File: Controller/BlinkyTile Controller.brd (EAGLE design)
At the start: 40 x 25 mm, 26 parts, among them CON1 USB_MICROSMT+THRUHULE, Q1 CRYSTAL_4PAD2520, U1 MK20D--VFM5, U2 W25Q80BV150, U3 74LVC1G17DCK, U4 74LVC1G17DCK, U5 74LVC1G17DCK

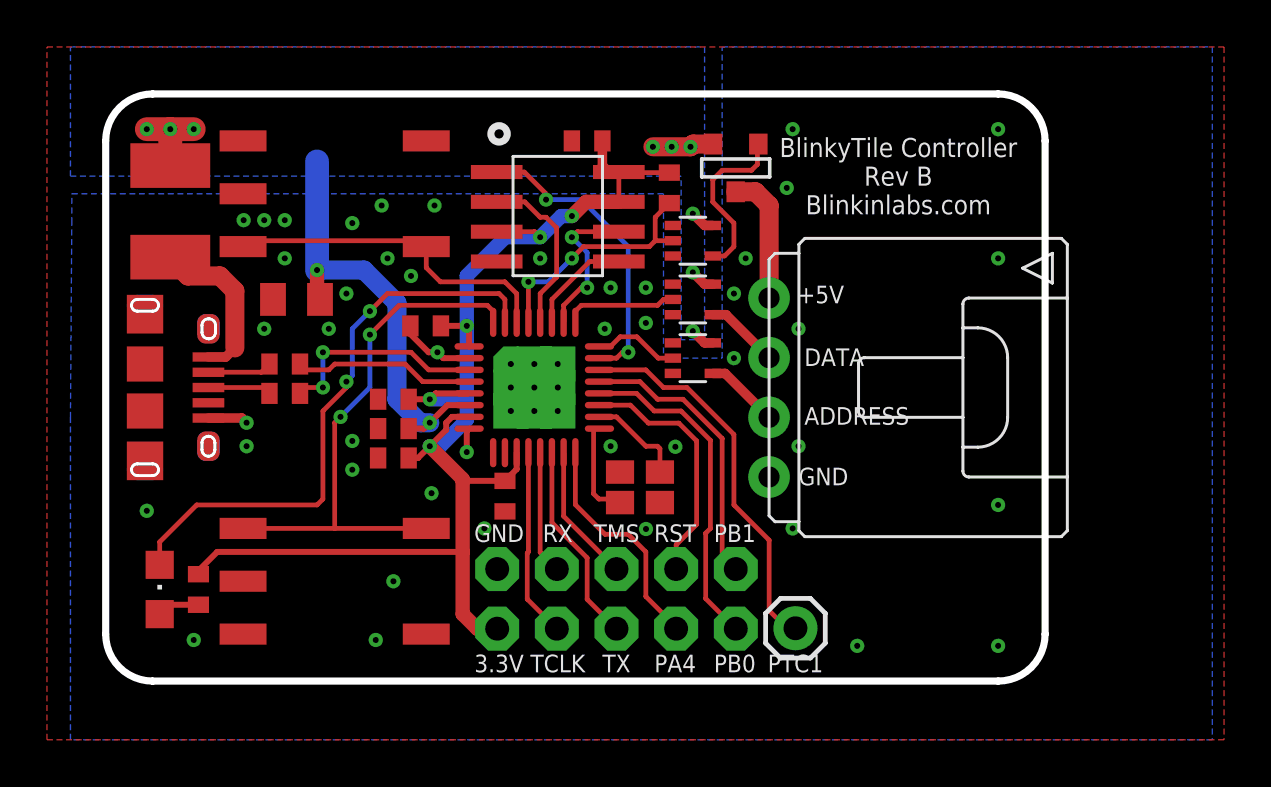
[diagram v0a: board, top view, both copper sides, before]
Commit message: Add ferrite beads, move the fuse to the ouput.
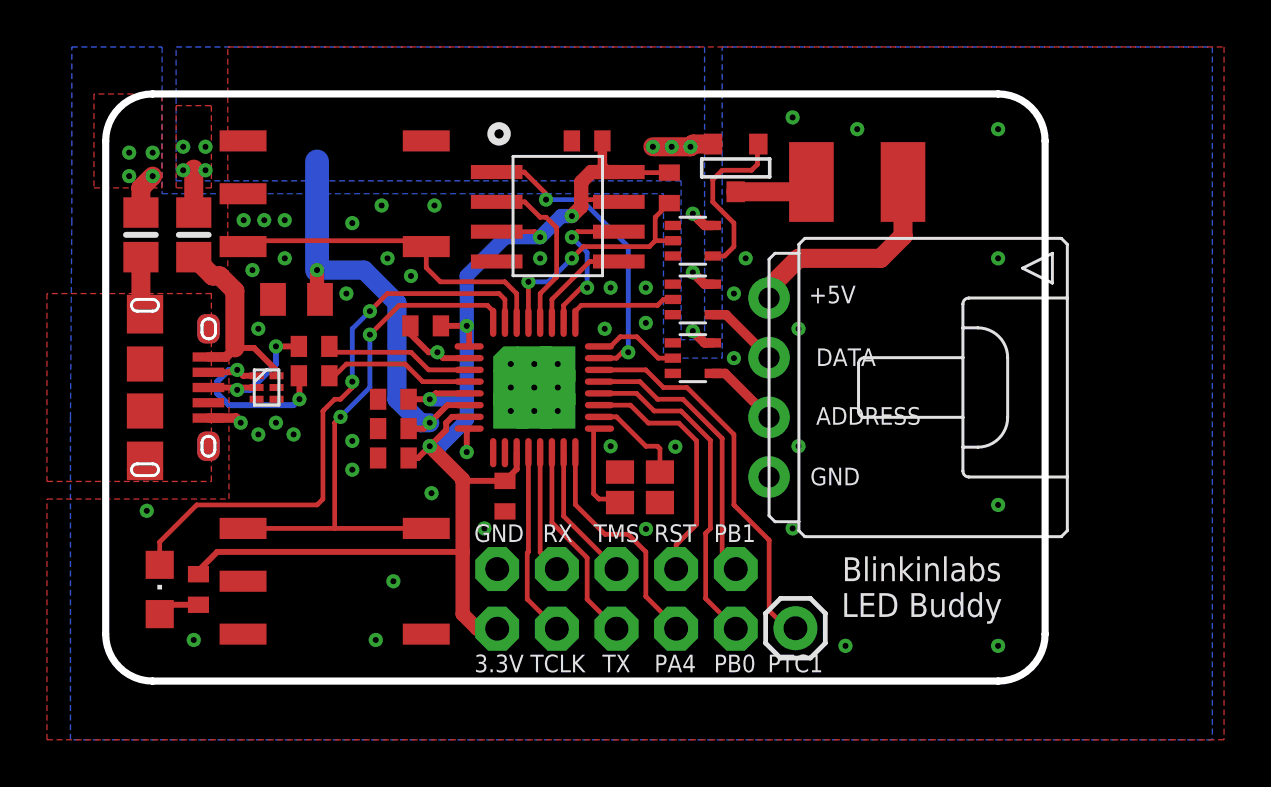
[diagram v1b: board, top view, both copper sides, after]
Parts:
- added L2, L3: FB0805/NO-OUTLINE, blinkinlabs:0805
- added U6: TPD4S012, blinkinlabs:R-PUSON-N6
- U2: value W25Q80BV150 -> W25Q--DVSN(150)
- moved L1 29.3 mm to (32.0, 8.75), turned to 0 degrees
- moved R2 2.36 mm to (8.88, 1.75)
- moved R1 1.35 mm to (8.88, 0.50)
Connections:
- removed net N$9: CON1.PIN$2, R1.1
- new net N$7: CON1.PIN$2, R1.1, U6.P$1
- new net N$8: L1.2, SV1.P$1
- new net SHIELD: CON1.PAD$1, CON1.PAD$10, CON1.PAD$2, CON1.PAD$3, CON1.PAD$4, CON1.PAD$5, CON1.PAD$6, CON1.PAD$7, CON1.PAD$8, CON1.PAD$9, L2.1
- net +5V: now also L3.1; no longer L1.2
- net GND: now also L2.2, U6.P$4
- net N$10: now also U6.P$2
- net N$3: now also L3.2, U6.P$6; no longer L1.1
- net N$5: now also L1.1; no longer SV1.P$1
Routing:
- net N$8: track 0.00 -> 9.35 mm
- net N$7: track 0.00 -> 8.57 mm, vias 0 -> 2
- net N$10: track 2.70 -> 5.96 mm, vias 0 -> 2
- net N$12: track 9.11 -> 6.36 mm, vias 2 -> 0
- net N$9: track 2.74 -> 0.00 mm
- net N$5: track 5.61 -> 3.40 mm
- net SHIELD: track 0.00 -> 2.12 mm
- net +5V: track 28.1 -> 26.4 mm, vias 11 -> 12
- net +3V3: track 57.3 -> 58.9 mm
- net GND: track 6.02 -> 7.53 mm, vias 45 -> 51
- net N$3: track 7.09 -> 8.46 mm
- net N$11: track 7.72 -> 6.47 mm
- added copper zone on layer 1, net +5V
- added copper zone on layer 1, net SHIELD
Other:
- board text added: "Blinkinlabs LED Buddy"
- board text added: "Blinkinlabs LED Buddy Rev C Blinkinlabs.com"
- board text removed: "BlinkyTile Controller Rev B Blinkinlabs.com"
- board text removed: "Thanks for using the BlinkyTile controller!"

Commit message: Tidy schematic and add values to ferrites, crystal
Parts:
- L2, L3: value FB0805/NO-OUTLINE -> 130ohm @100MHz
- Q1: value CRYSTAL_4PAD2520 -> 16MHz
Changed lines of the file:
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@@
 <attribute name="VALUE" x="4.84" y="-9.87" size="1.27" layer="27" rot="R90"/>
 </element>
-<element name="Q1" library="blinkinlabs" package="CRSYTAL_2520" value="CRYSTAL_4PAD2520" x="22.75" y="-4.25" smashed="yes" rot="R180"/>
+<element name="Q1" library="blinkinlabs" package="CRSYTAL_2520" value="16MHz" x="22.75" y="-4.25" smashed="yes" rot="R180"/>
 <element name="R1" library="adafruit" package="R0402" value="33" x="8.875" y="0.5" smashed="yes"/>
 <element name="R2" library="adafruit" package="R0402" value="33" x="8.875" y="1.75" smashed="yes"/>
@@
 <attribute name="VALUE" x="4.405" y="1.905" size="1.27" layer="27" ratio="10" rot="R270"/>
 </element>
-<element name="L3" library="blinkinlabs" package="0805" value="FB0805/NO-OUTLINE" x="3.75" y="6.5" smashed="yes" rot="R270">
+<element name="L3" library="blinkinlabs" package="0805" value="130ohm @100MHz" x="3.75" y="6.5" smashed="yes" rot="R270">
 <attribute name="VALUE" x="2.988" y="4.468" size="0.4064" layer="27" ratio="10" rot="R270"/>
 </element>
-<element name="L2" library="blinkinlabs" package="0805" value="FB0805/NO-OUTLINE" x="1.5" y="6.5" smashed="yes" rot="R90">
+<element name="L2" library="blinkinlabs" package="0805" value="130ohm @100MHz" x="1.5" y="6.5" smashed="yes" rot="R90">
 <attribute name="VALUE" x="2.262" y="8.532" size="0.4064" layer="27" ratio="10" rot="R90"/>
 </element>

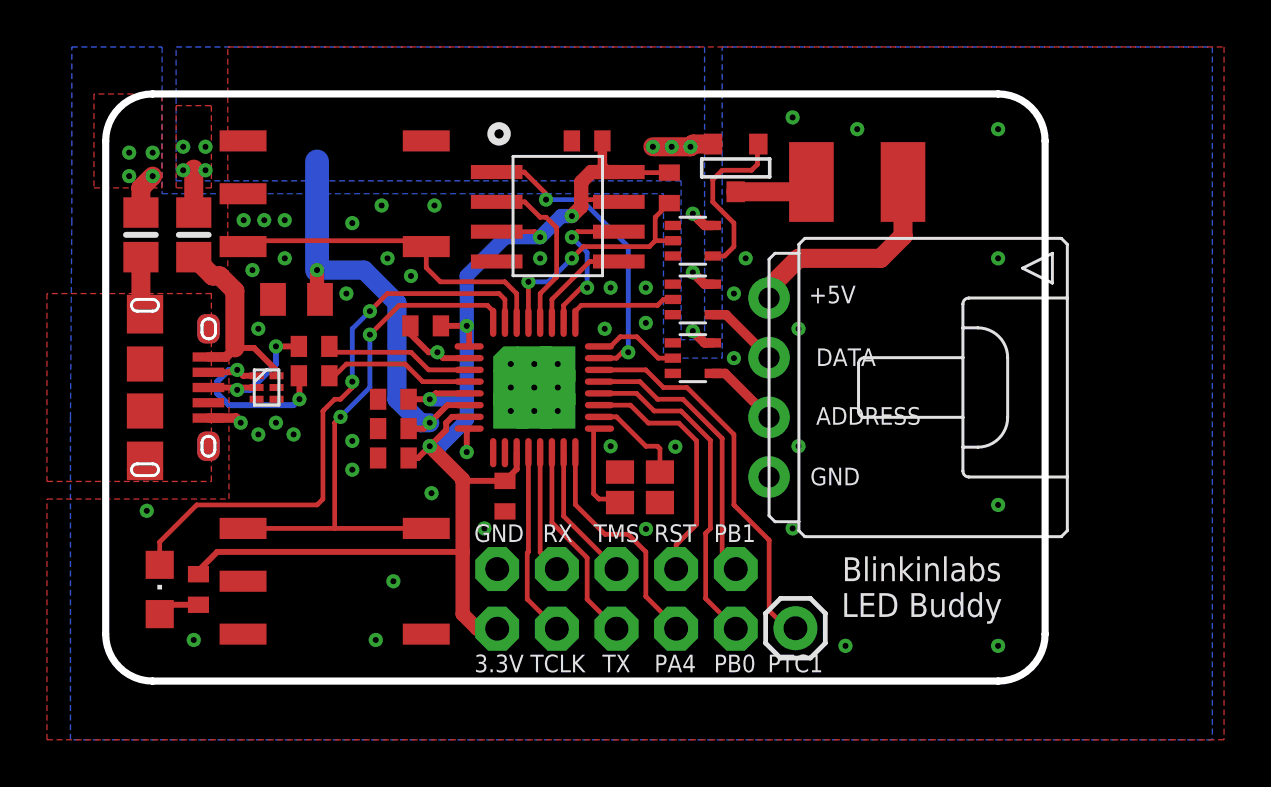
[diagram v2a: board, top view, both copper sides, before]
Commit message: Enlarge via sizes to .3mm
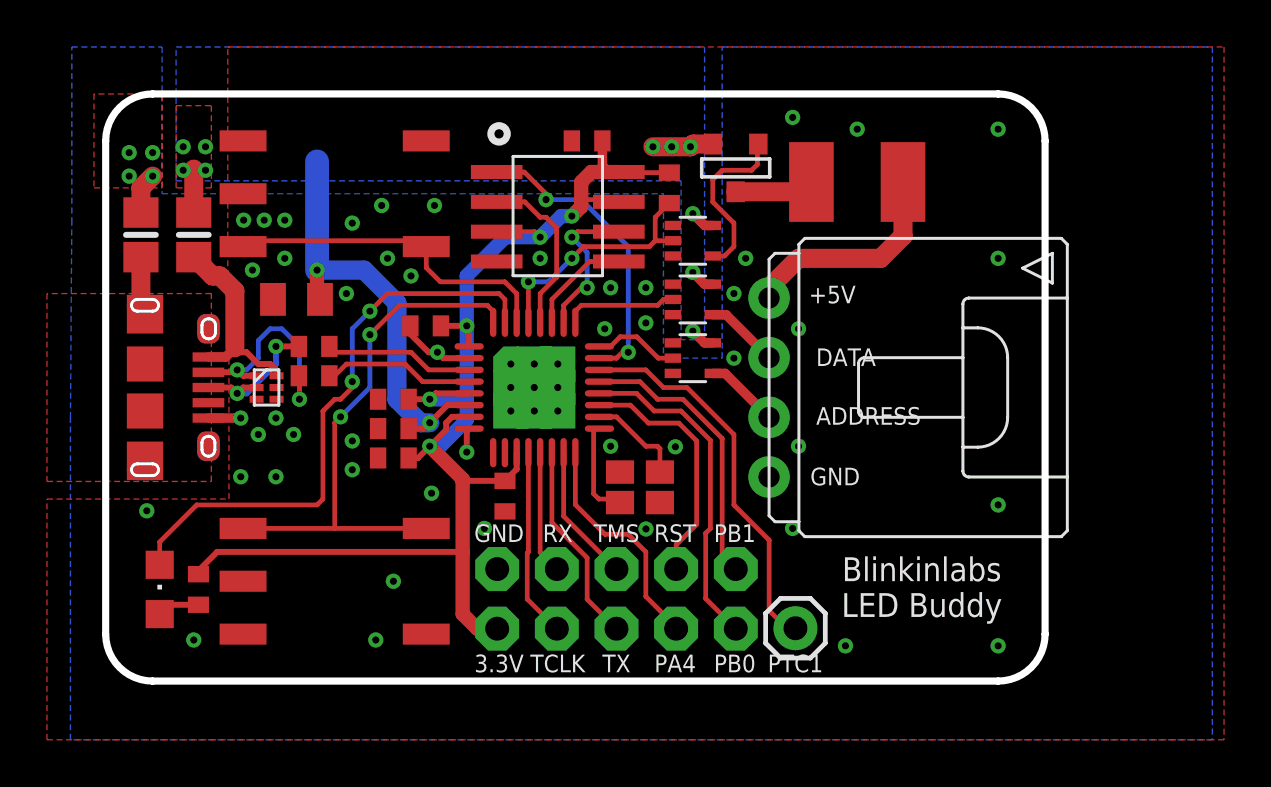
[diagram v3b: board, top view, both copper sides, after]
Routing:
- net N$7: track 8.57 -> 9.58 mm
- net GND: track 7.53 -> 7.45 mm, vias 51 -> 52

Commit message: Controller: Switch back to 208 package for flash chip
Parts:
- U2: value W25Q--DVSN(150) -> W25Q--DVSS(208); device blinkinlabs:SOIC8-150 -> blinkinlabs:SOIC8-208
- moved U2 0.15 mm to (19.1, 7.30)
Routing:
- net +3V3: track 58.9 -> 61.1 mm
- net FLASH_MISO: track 7.67 -> 9.55 mm
- net GND: track 7.45 -> 9.27 mm
- net FLASH_CS: track 12.9 -> 13.8 mm
- net FLASH_SCK: track 6.55 -> 7.19 mm
- net FLASH_MOSI: track 4.49 -> 5.13 mm
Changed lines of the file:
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@@
 <element name="R2" library="adafruit" package="R0402" value="33" x="8.875" y="1.75" smashed="yes"/>
 <element name="R4" library="adafruit" package="R0402" value="330" x="3.95" y="-8.6" smashed="yes" rot="R90"/>
-<element name="U2" library="blinkinlabs" package="SOIC8-150" value="W25Q--DVSN(150)" x="19.25" y="7.3" smashed="yes" rot="R270"/>
+<element name="U2" library="blinkinlabs" package="SOIC8-208" value="W25Q--DVSS(208)" x="19.1" y="7.3" smashed="yes" rot="R270"/>
 <element name="CON1" library="blinkinlabs" package="USB_MICRO_THRUHOLE" value="USB_MICROSMT+THRUHULE" x="1.675" y="0" smashed="yes" rot="R270"/>
 <element name="U4" library="74xx-little-us" package="SC70-5" value="74LVC1G17DCK" x="25" y="3.75" smashed="yes" rot="R270"/>
@@
 <via x="7.25" y="-3.8" extent="1-16" drill="0.3"/>
 <via x="5.75" y="-3.8" extent="1-16" drill="0.3"/>
+<wire x1="24.15" y1="5.6" x2="24.15" y2="5.4" width="0.2032" layer="1"/>
+<wire x1="24.15" y1="5.4" x2="23" y2="4.25" width="0.2032" layer="1"/>
 </signal>
 <signal name="N$2">
@@
 <wire x1="14.5" y1="-1.5" x2="14.5" y2="-1.8" width="0.254" layer="1"/>
 <wire x1="14.5" y1="-1.8" x2="13.8" y2="-2.5" width="0.254" layer="1"/>
-<wire x1="21.85" y1="9.175" x2="21.425" y2="9.175" width="0.4064" layer="1"/>
+<wire x1="22.49" y1="9.175" x2="21.425" y2="9.175" width="0.4064" layer="1"/>
 <wire x1="17.5" y1="-2.775" x2="17.5" y2="-3.475" width="0.254" layer="1"/>
 <wire x1="17.5" y1="-3.475" x2="17" y2="-3.975" width="0.254" layer="1"/>
@@
 <wire x1="15.81975" y1="-10.27" x2="15.2" y2="-9.65025" width="0.6096" layer="1"/>
 <via x="19.85" y="7.3" extent="1-16" drill="0.3"/>
-<wire x1="16.65" y1="6.635" x2="18.265" y2="6.635" width="0.2032" layer="1"/>
+<wire x1="15.71" y1="6.635" x2="18.265" y2="6.635" width="0.2032" layer="1"/>
 <wire x1="18.265" y1="6.635" x2="18.5" y2="6.4" width="0.2032" layer="1"/>
 <wire x1="19.85" y1="7.3" x2="19.4" y2="7.3" width="0.6096" layer="16"/>
@@
 <wire x1="15.375" y1="4.76" x2="17.015" y2="6.4" width="0.6096" layer="16"/>
 <wire x1="17.015" y1="6.4" x2="18.5" y2="6.4" width="0.6096" layer="16"/>
-<wire x1="21.85" y1="9.175" x2="21.875" y2="9.15" width="0.2032" layer="1"/>
-<wire x1="21.875" y1="9.15" x2="24" y2="9.15" width="0.2032" layer="1"/>
 <wire x1="21.425" y1="9.175" x2="21.15" y2="9.45" width="0.4064" layer="1"/>
 <wire x1="21.15" y1="9.45" x2="21.15" y2="10.5" width="0.4064" layer="1"/>
@@
 <wire x1="20.25" y1="8" x2="20.25" y2="8.75" width="0.6096" layer="1"/>
 <wire x1="20.25" y1="8.75" x2="20.675" y2="9.175" width="0.6096" layer="1"/>
-<wire x1="20.675" y1="9.175" x2="21.85" y2="9.175" width="0.6096" layer="1"/>
-<wire x1="21.85" y1="7.905" x2="21.755" y2="8" width="0.2032" layer="1"/>
-<wire x1="21.755" y1="8" x2="20.25" y2="8" width="0.2032" layer="1"/>
+<wire x1="20.675" y1="9.175" x2="22.49" y2="9.175" width="0.6096" layer="1"/>
+<wire x1="22.49" y1="9.175" x2="23.975" y2="9.175" width="0.2032" layer="1"/>
+<wire x1="23.975" y1="9.175" x2="24" y2="9.15" width="0.2032" layer="1"/>
+<wire x1="22.49" y1="7.905" x2="20.345" y2="7.905" width="0.2032" layer="1"/>
+<wire x1="20.345" y1="7.905" x2="20.25" y2="8" width="0.2032" layer="1"/>
 </signal>
 <signal name="TCLK">
@@
 <wire x1="22.25" y1="6" x2="20.25" y2="8" width="0.2032" layer="16"/>
 <wire x1="20.25" y1="8" x2="18.75" y2="8" width="0.2032" layer="16"/>
-<wire x1="16.65" y1="9.175" x2="17.825" y2="9.175" width="0.2032" layer="1"/>
+<wire x1="15.71" y1="9.175" x2="17.825" y2="9.175" width="0.2032" layer="1"/>
 <wire x1="17.825" y1="9.175" x2="18.75" y2="8.25" width="0.2032" layer="1"/>
 <wire x1="18.75" y1="8.25" x2="18.75" y2="8" width="0.2032" layer="1"/>
@@
 <via x="20.5" y="4.25" extent="1-16" drill="0.3"/>
 <via x="19.85" y="6.4" extent="1-16" drill="0.3"/>
-<wire x1="21.85" y1="6.635" x2="20.085" y2="6.635" width="0.2032" layer="1"/>
+<wire x1="22.49" y1="6.635" x2="20.085" y2="6.635" width="0.2032" layer="1"/>
 <wire x1="20.085" y1="6.635" x2="19.85" y2="6.4" width="0.2032" layer="1"/>
 <wire x1="20.5" y1="4.25" x2="20.5" y2="5.75" width="0.2032" layer="16"/>
@@
 <wire x1="19" y1="2.775" x2="19" y2="3.75" width="0.2032" layer="1"/>
 <wire x1="19" y1="3.75" x2="20.615" y2="5.365" width="0.2032" layer="1"/>
-<wire x1="21.85" y1="5.365" x2="20.615" y2="5.365" width="0.2032" layer="1"/>
+<wire x1="22.49" y1="5.365" x2="20.615" y2="5.365" width="0.2032" layer="1"/>
 </signal>
 <signal name="FLASH_MISO">
 <contactref element="U2" pad="2"/>
 <contactref element="U1" pad="28"/>
-<wire x1="17" y1="7.905" x2="16.65" y2="7.905" width="0.2032" layer="1"/>
+<wire x1="17" y1="7.905" x2="15.71" y2="7.905" width="0.2032" layer="1"/>
 <wire x1="18.5" y1="2.775" x2="18.5" y2="4" width="0.2032" layer="1"/>
 <wire x1="19.2" y1="4.7" x2="19.2" y2="6.8" width="0.2032" layer="1"/>
@@
 <wire x1="18.75" y1="7.25" x2="18.5" y2="7.25" width="0.2032" layer="1"/>
 <wire x1="18.5" y1="7.25" x2="17.845" y2="7.905" width="0.2032" layer="1"/>
-<wire x1="16.65" y1="7.905" x2="17.845" y2="7.905" width="0.2032" layer="1"/>
+<wire x1="15.71" y1="7.905" x2="17.845" y2="7.905" width="0.2032" layer="1"/>
 </signal>
 <signal name="STATUS">
@@
 <contactref element="R5" pad="1"/>
 <wire x1="18" y1="4.5" x2="18" y2="2.775" width="0.2032" layer="1"/>
-<wire x1="23.15" y1="6" x2="23.4" y2="6.25" width="0.2032" layer="1"/>
-<wire x1="23.4" y1="6.25" x2="24.15" y2="6.25" width="0.2032" layer="1"/>
-<wire x1="23.15" y1="6" x2="20.35" y2="6" width="0.2032" layer="1"/>
+<wire x1="23.45" y1="6.25" x2="24.15" y2="6.25" width="0.2032" layer="1"/>
 <wire x1="20.35" y1="6" x2="19.85" y2="5.5" width="0.2032" layer="1"/>
 <wire x1="18" y1="4.5" x2="18.85" y2="4.5" width="0.2032" layer="16"/>
 <wire x1="18.85" y1="4.5" x2="19.85" y2="5.5" width="0.2032" layer="16"/>
-<wire x1="24" y1="7.85" x2="23.4" y2="7.25" width="0.2032" layer="1"/>
-<wire x1="23.4" y1="7.25" x2="23.4" y2="6.25" width="0.2032" layer="1"/>
+<wire x1="23.45" y1="7.3" x2="23.45" y2="6.25" width="0.2032" layer="1"/>
+<wire x1="20.35" y1="6" x2="23.45" y2="6" width="0.2032" layer="1"/>
+<wire x1="23.45" y1="7.3" x2="24" y2="7.85" width="0.2032" layer="1"/>
+<wire x1="23.45" y1="6.25" x2="23.45" y2="6" width="0.2032" layer="1"/>
 </signal>
 <signal name="N$6">
